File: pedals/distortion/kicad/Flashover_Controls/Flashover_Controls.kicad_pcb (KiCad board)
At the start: 2 copper layers, 84 x 58 mm, 68 parts, among them J8 To main board, SW1 PEC11R-4215F-S0024, SW2 PEC11R-4215F-S0024, SW3 PEC11R-4215F-S0024, SW4 Soft/Hard, U10 IS31FL3236A

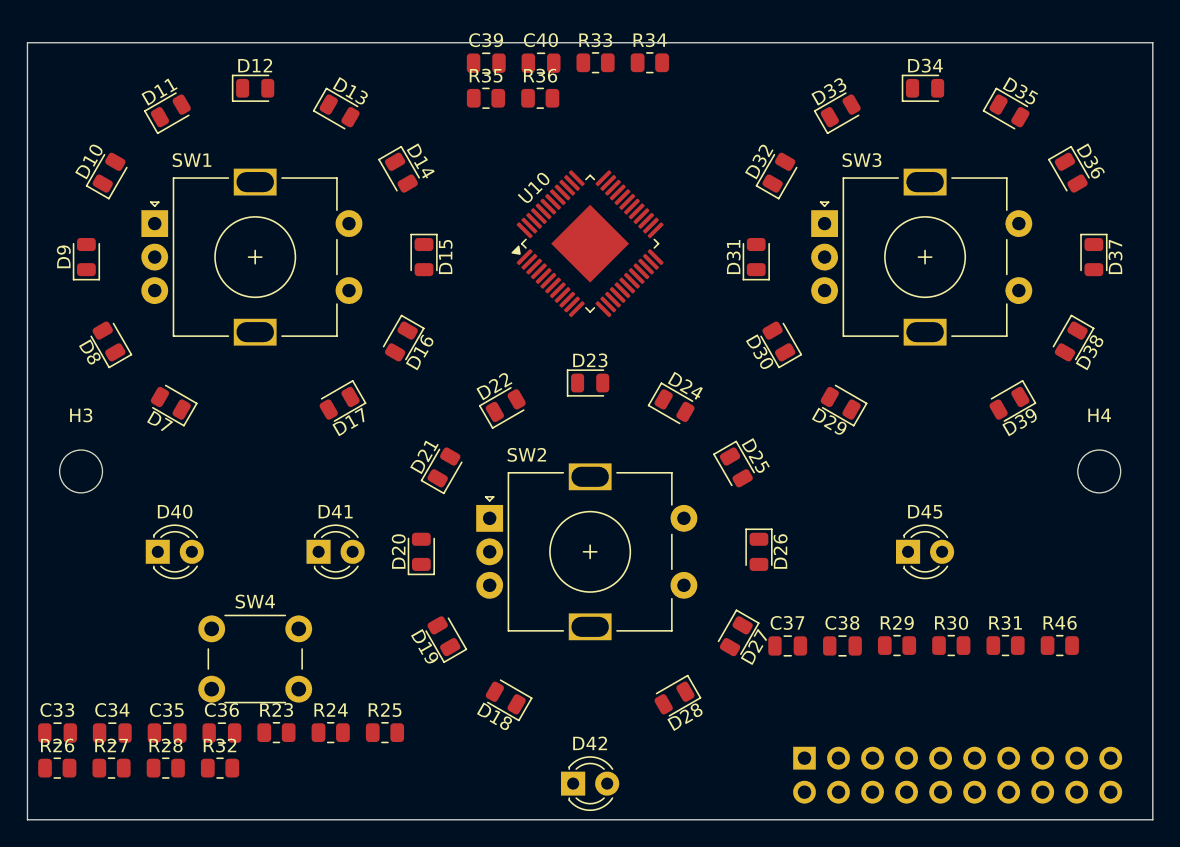
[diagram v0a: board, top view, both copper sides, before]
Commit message: Route Flashover boards (partial); add status note
Both boards now 4-layer with inner ground (and +5V) planes, JLCPCB-style
rules and net classes, ground/+5V via fan-out and autorouted signals.
Control board: 7 connections open.  Main board: 50 open; to be finished
by hand.  See pedals/distortion/kicad/FLASHOVER_STATUS.md.

Co-Authored-By: Claude Opus 5.5 <noreply@anthropic.com>
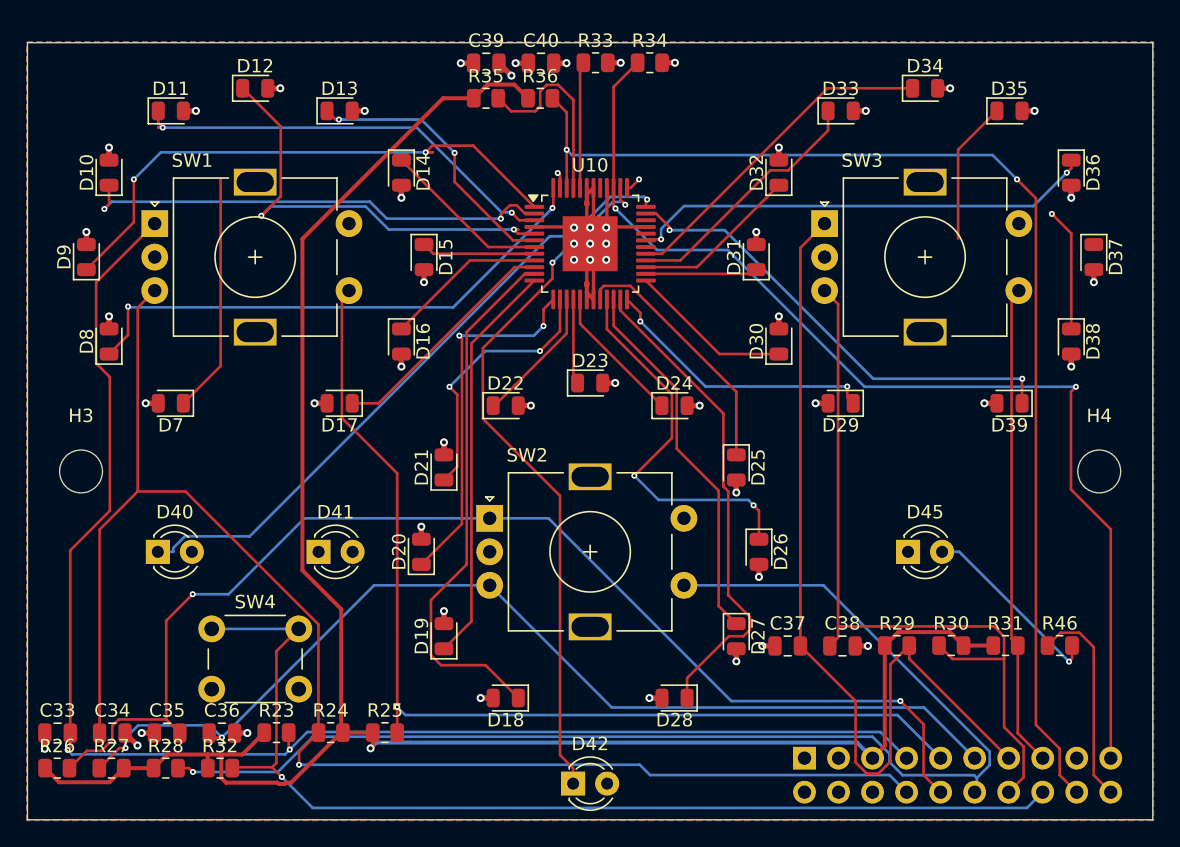
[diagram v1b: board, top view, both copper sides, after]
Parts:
- turned D10 to 90 degrees
- turned D21 to 90 degrees
- turned D32 to 90 degrees
- turned D11 to 0 degrees
- turned D13 to 0 degrees
- turned D19 to 90 degrees
- turned D22 to 0 degrees
- turned D24 to 0 degrees
- turned D30 to 90 degrees
- turned D33 to 0 degrees
- turned D35 to 0 degrees
- turned D8 to 90 degrees
- turned D14 to -90 degrees
- turned D25 to -90 degrees
- turned D36 to -90 degrees
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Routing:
- net +3V3: track 0.00 -> 151.6 mm, vias 0 -> 1
- net GAIN_B: track 0.00 -> 109.6 mm, vias 0 -> 1
- net GAIN_A: track 0.00 -> 108.4 mm, vias 0 -> 2
- net TONE_SW: track 0.00 -> 93.9 mm, vias 0 -> 1
- net TONE_A: track 0.00 -> 89.8 mm, vias 0 -> 2
- net LED_SCL: track 0.00 -> 89.2 mm, vias 0 -> 2
- net LED_EN: track 0.00 -> 80.7 mm, vias 0 -> 2
- net MODE_BTN: track 0.00 -> 79.9 mm, vias 0 -> 1
- net TONE_B: track 0.00 -> 78.6 mm, vias 0 -> 2
- net GAIN_SW: track 0.00 -> 77.1 mm, vias 0 -> 1
- net LEVEL_A: track 0.00 -> 66.7 mm
- net LEVEL_B: track 0.00 -> 57.9 mm
- net /LED Rings/ON: track 0.00 -> 53.5 mm, vias 0 -> 2
- net /LED Rings/SOFT: track 0.00 -> 48.6 mm, vias 0 -> 1
- net /LED Rings/G3: track 0.00 -> 43.0 mm, vias 0 -> 2
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- added copper zone on In2.Cu, net +5V
- added copper zone on B.Cu, net GND
- added copper zone on F.Cu, net GND
- added copper zone on In1.Cu, net GND
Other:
- copper layers 2 -> 4

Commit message: Hand-route two Flashover control board connections
U10 +5V (pad 41) via to the +5V plane, and HARD to D41 on B.Cu.
5 connections left. drc.sh now refills zones before checking.

Co-Authored-By: Claude Opus 5.5 <noreply@anthropic.com>
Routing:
- net /LED Rings/HARD: track 1.16 -> 67.3 mm
- net +5V: track 38.5 -> 40.4 mm, vias 35 -> 36
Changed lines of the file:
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@@
 	)
 	(segment
+		(start 147.75 90.8375)
+		(end 147.75 89.0832)
+		(width 0.4)
+		(layer "F.Cu")
+		(net "+5V")
+	)
+	(segment
 		(start 132.912 103.7065)
 		(end 132.9119 103.7064)
@@
 	)
 	(segment
+		(start 147.75 89.0832)
+		(end 147.6 88.9332)
+		(width 0.4)
+		(layer "F.Cu")
+		(net "+5V")
+	)
+	(segment
 		(start 111.0881 100.8936)
 		(end 111.0881 101.3625)
@@
 	)
 	(via
+		(at 147.6 88.9332)
+		(size 0.6)
+		(drill 0.3)
+		(layers "F.Cu" "B.Cu")
+		(net "+5V")
+	)
+	(via
 		(at 134.6 97.875)
 		(size 0.6)
@@
 		(net "/LED Rings/HARD")
 	)
+	(segment
+		(start 147.734626 90.2006)
+		(end 121.436926 116.4983)
+		(width 0.2)
+		(layer "B.Cu")
+		(net "/LED Rings/HARD")
+	)
+	(segment
+		(start 121.436926 116.4983)
+		(end 113.9317 116.4983)
+		(width 0.2)
+		(layer "B.Cu")
+		(net "/LED Rings/HARD")
+	)
+	(segment
+		(start 123.092 121.638)
+		(end 126.73 118)
+		(width 0.2)
+		(layer "B.Cu")
+		(net "/LED Rings/HARD")
+	)
+	(segment
+		(start 113.58 116.85)
+		(end 113.58 119.15)
+		(width 0.2)
+		(layer "B.Cu")
+		(net "/LED Rings/HARD")
+	)
+	(segment
+		(start 113.58 119.15)
+		(end 116.068 121.638)
+		(width 0.2)
+		(layer "B.Cu")
+		(net "/LED Rings/HARD")
+	)
+	(segment
+		(start 116.068 121.638)
+		(end 123.092 121.638)
+		(width 0.2)
+		(layer "B.Cu")
+		(net "/LED Rings/HARD")
+	)
+	(segment
+		(start 113.9317 116.4983)
+		(end 113.58 116.85)
+		(width 0.2)
+		(layer "B.Cu")
+		(net "/LED Rings/HARD")
+	)
+	(segment
+		(start 150.6479 90.2006)
+		(end 147.734626 90.2006)
+		(width 0.2)
+		(layer "B.Cu")
+		(net "/LED Rings/HARD")
+	)

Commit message: Finish routing the Flashover control board by hand
All connections routed (L7, L9, L10, G1, LED_SDA by hand) and the
autorouter's leftover track stubs removed. DRC: 0 unconnected, 0 errors,
schematic parity clean; only silkscreen warnings remain.

Co-Authored-By: Claude Opus 5.5 <noreply@anthropic.com>
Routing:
- net LED_SDA: track 14.5 -> 112.3 mm, vias 0 -> 1
- net /LED Rings/L7: track 10.7 -> 81.7 mm, vias 0 -> 2
- net /LED Rings/L9: track 0.00 -> 57.1 mm, vias 0 -> 2
- net /LED Rings/G1: track 19.0 -> 64.3 mm, vias 1 -> 2
- net /LED Rings/L10: track 9.18 -> 51.2 mm, vias 1 -> 2
- net /LED Rings/G3: track 43.0 -> 41.0 mm
- net /LED Rings/G5: track 33.3 -> 32.0 mm

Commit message: Fit Flashover to the 1590BB and part datasheets
- Correct PEC11R encoder footprint (legs 13.2 mm apart) in a new
  GreywireStudio footprint library; swap it onto the control board and
  bend three tracks around the wider legs
- Move MIDI jacks to the side walls, spread the top jacks out and put
  their fronts against the wall; re-autoroute the main board
- gen_pcb.py rebuilds the control board only with --controls
- Add fit check, board heights and drilling guide to the status note;
  update the product document

Co-Authored-By: Claude Opus 5.5 <noreply@anthropic.com>
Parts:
- SW1, SW2, SW3: value PEC11R-4215F-S0024 -> PEC11R-4220F-S0024; footprint Rotary_Encoder:RotaryEncoder_Alps_EC11E-Switch_Vertical_H20mm -> GreywireStudio:RotaryEncoder_Bourns_PEC11R-4xxxF-Sxxxx_Vertical
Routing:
- net LED_SDA: track 112.3 -> 115.2 mm
- net LED_SCL: track 89.2 -> 90.7 mm
- net /LED Rings/G3: track 41.0 -> 41.6 mm
